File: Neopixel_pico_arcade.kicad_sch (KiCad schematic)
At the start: 15 parts, among them J1 SWD_connector, J2 NES_controller_connector, J3 USB_C_Receptacle_USB2.0, Q1 2N7002, U1 RP2040_Stamp, U2 SN74LV1T34DBV, U3 SRV05-4HTG-D

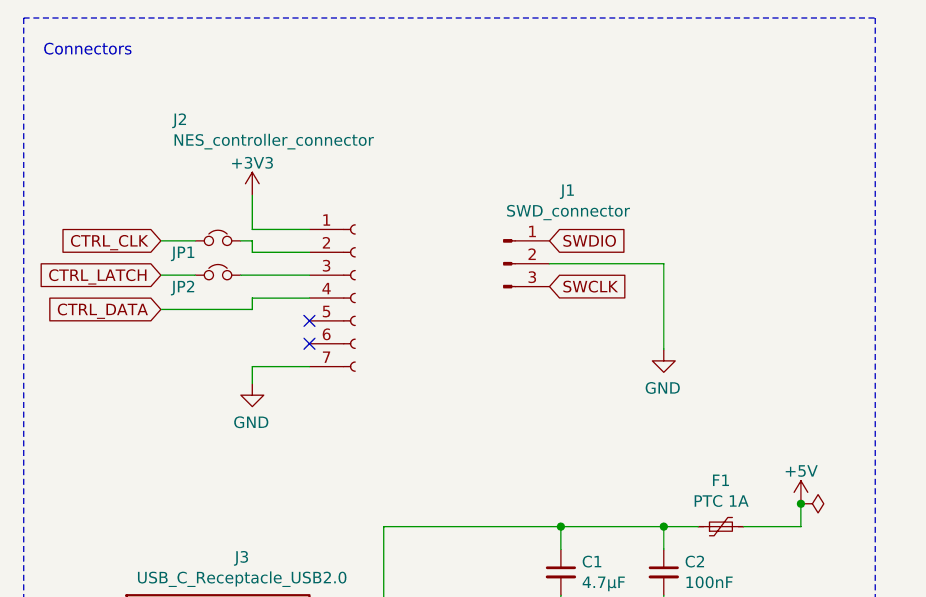
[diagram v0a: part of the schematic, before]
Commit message: Adds custom schematic symbol for NES controller connector
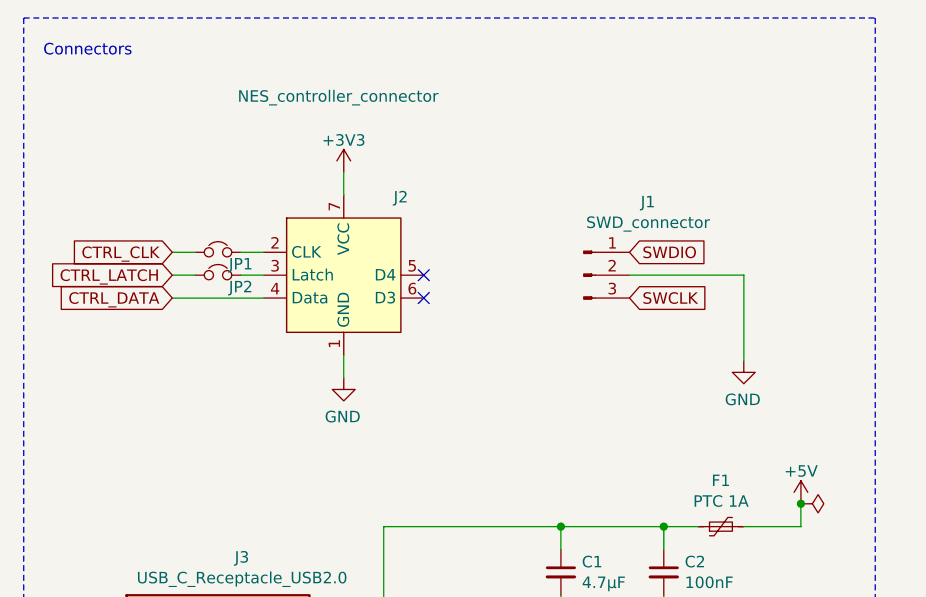
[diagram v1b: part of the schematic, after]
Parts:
- removed J2: NES_controller_connector, symbol Connector:Conn_01x07_Female
- added J2: NES_controller_connector, symbol Neopixel_pico_arcade:NES_controller_connector
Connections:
- net +3V3: now also J2.7 (VCC)
- net CTRL_DATA: now also J2.4 (Data)
- net GND: now also J2.1 (GND)
- net at JP1.2: now also J2.2 (CLK)
- net at JP2.2: now also J2.3 (Latch)
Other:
- moved on the sheet: J1, JP1

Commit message: Adds footprint for the NES controller connector
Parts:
- J2: footprint (none) -> Neopixel_pico_arcade:NES_Controller_connector
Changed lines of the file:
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@@
     (property "Reference" "J2" (id 0) (at 60.96 38.3244 0))
     (property "Value" "NES_controller_connector" (id 1) (at 53.975 27.1295 0))
-    (property "Footprint" "" (id 2) (at 54.61 46.99 0)
+    (property "Footprint" "Neopixel_pico_arcade:NES_Controller_connector" (id 2) (at 54.61 46.99 0)
       (effects (font (size 1.27 1.27)) hide)
     )
@@
     )
     (path "/0d864839-2792-4de0-80be-2a96e9fb5773"
-      (reference "J2") (unit 1) (value "NES_controller_connector") (footprint "")
+      (reference "J2") (unit 1) (value "NES_controller_connector") (footprint "Neopixel_pico_arcade:NES_Controller_connector")
     )
     (path "/6c963e39-9c66-450d-9ace-cb36b00aa8c0"

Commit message: Reassociates RP2040 stamp to the footprint
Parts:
- U1: footprint RP2040_Stamp:RP2040_Stamp_SMD -> RP2040_stamp:RP2040_Stamp_SMD
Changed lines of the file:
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@@
     (property "Reference" "U1" (id 0) (at 158.75 36.7242 0))
     (property "Value" "RP2040_Stamp" (id 1) (at 158.75 39.4993 0))
-    (property "Footprint" "RP2040_Stamp:RP2040_Stamp_SMD" (id 2) (at 158.75 123.19 0)
+    (property "Footprint" "RP2040_stamp:RP2040_Stamp_SMD" (id 2) (at 158.75 123.19 0)
       (effects (font (size 1.27 1.27)) hide)
     )
@@
     )
     (path "/99fe8e35-e5c1-4239-bd41-6a284ef403a7"
-      (reference "U1") (unit 1) (value "RP2040_Stamp") (footprint "RP2040_Stamp:RP2040_Stamp_SMD")
+      (reference "U1") (unit 1) (value "RP2040_Stamp") (footprint "RP2040_stamp:RP2040_Stamp_SMD")
     )
     (path "/9cc9bd3c-cb16-401b-a7ae-599f0e3ee9ec"

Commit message: Adds footprint for GTC USB4105 USB type C connector
This connector is for USB2.0 and power delivery only.

Datasheet is available at https://gct.co/files/specs/usb4105-spec.pdf
and drawings at https://gct.co/files/drawings/usb4105.pdf
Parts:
- J3: footprint Neopixel_pico_arcade:USB_C_Receptacle_JAE_DX07S016JA1 -> Neopixel_pico_arcade:USB_C_Receptacle_USB_2_GTC_USB4105
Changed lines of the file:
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@@
     (property "Reference" "J3" (id 0) (at 43.307 78.3398 0))
     (property "Value" "USB_C_Receptacle_USB2.0" (id 1) (at 43.307 80.6385 0))
-    (property "Footprint" "Neopixel_pico_arcade:USB_C_Receptacle_JAE_DX07S016JA1" (id 2) (at 44.45 100.33 0)
+    (property "Footprint" "Neopixel_pico_arcade:USB_C_Receptacle_USB_2_GTC_USB4105" (id 2) (at 44.45 100.33 0)
       (effects (font (size 1.27 1.27)) hide)
     )
@@
     )
     (path "/6c963e39-9c66-450d-9ace-cb36b00aa8c0"
-      (reference "J3") (unit 1) (value "USB_C_Receptacle_USB2.0") (footprint "Neopixel_pico_arcade:USB_C_Receptacle_JAE_DX07S016JA1")
+      (reference "J3") (unit 1) (value "USB_C_Receptacle_USB2.0") (footprint "Neopixel_pico_arcade:USB_C_Receptacle_USB_2_GTC_USB4105")
     )
     (path "/a9c99e6b-55b1-4adc-8611-0aea35c1c656"

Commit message: Adds project name and revision to schematics
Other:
- title: (none) -> Neopixel pico arcade
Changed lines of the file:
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@@
 (kicad_sch (version 20210621) (generator eeschema)
   (paper "A4")
+  (title_block
+    (title "Neopixel pico arcade")
+    (rev "1.0")
+  )
   (junction (at 36.83 127) (diameter 1.016) (color 0 0 0 0))
   (junction (at 57.15 100.33) (diameter 1.016) (color 0 0 0 0))

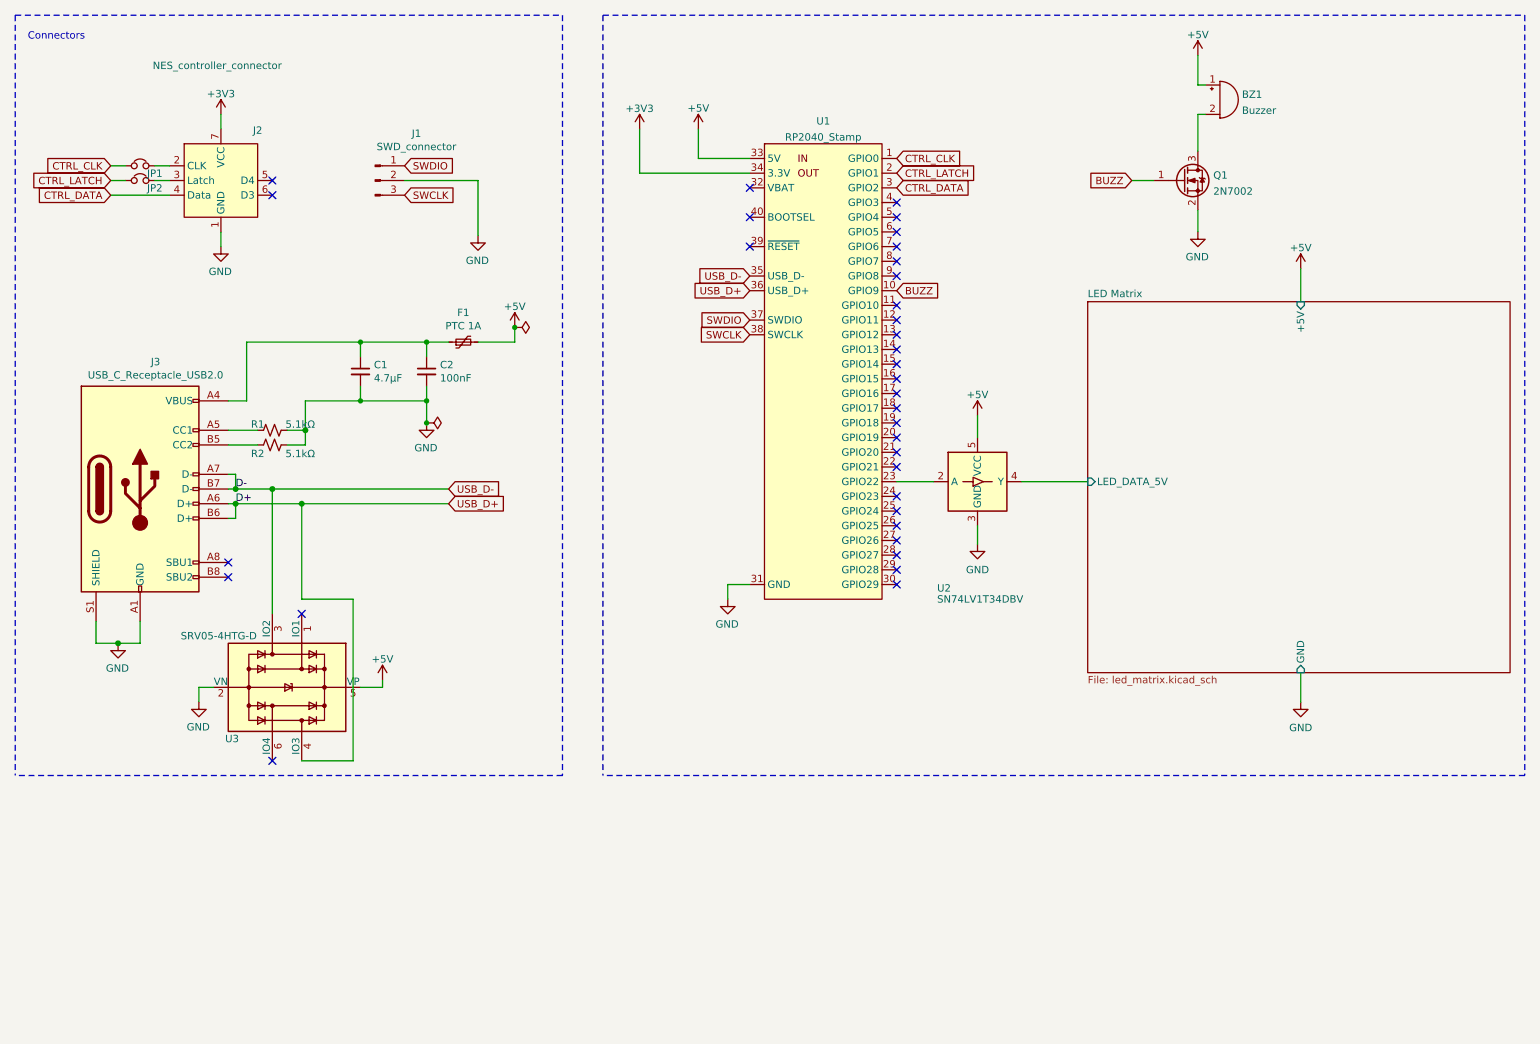
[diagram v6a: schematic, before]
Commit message: Adds mounting holes to schematics
These are connected to ground, but will have pads only on once the
bottom so the exposed pad on top doesn't interfere with the face where
the LEDs are.
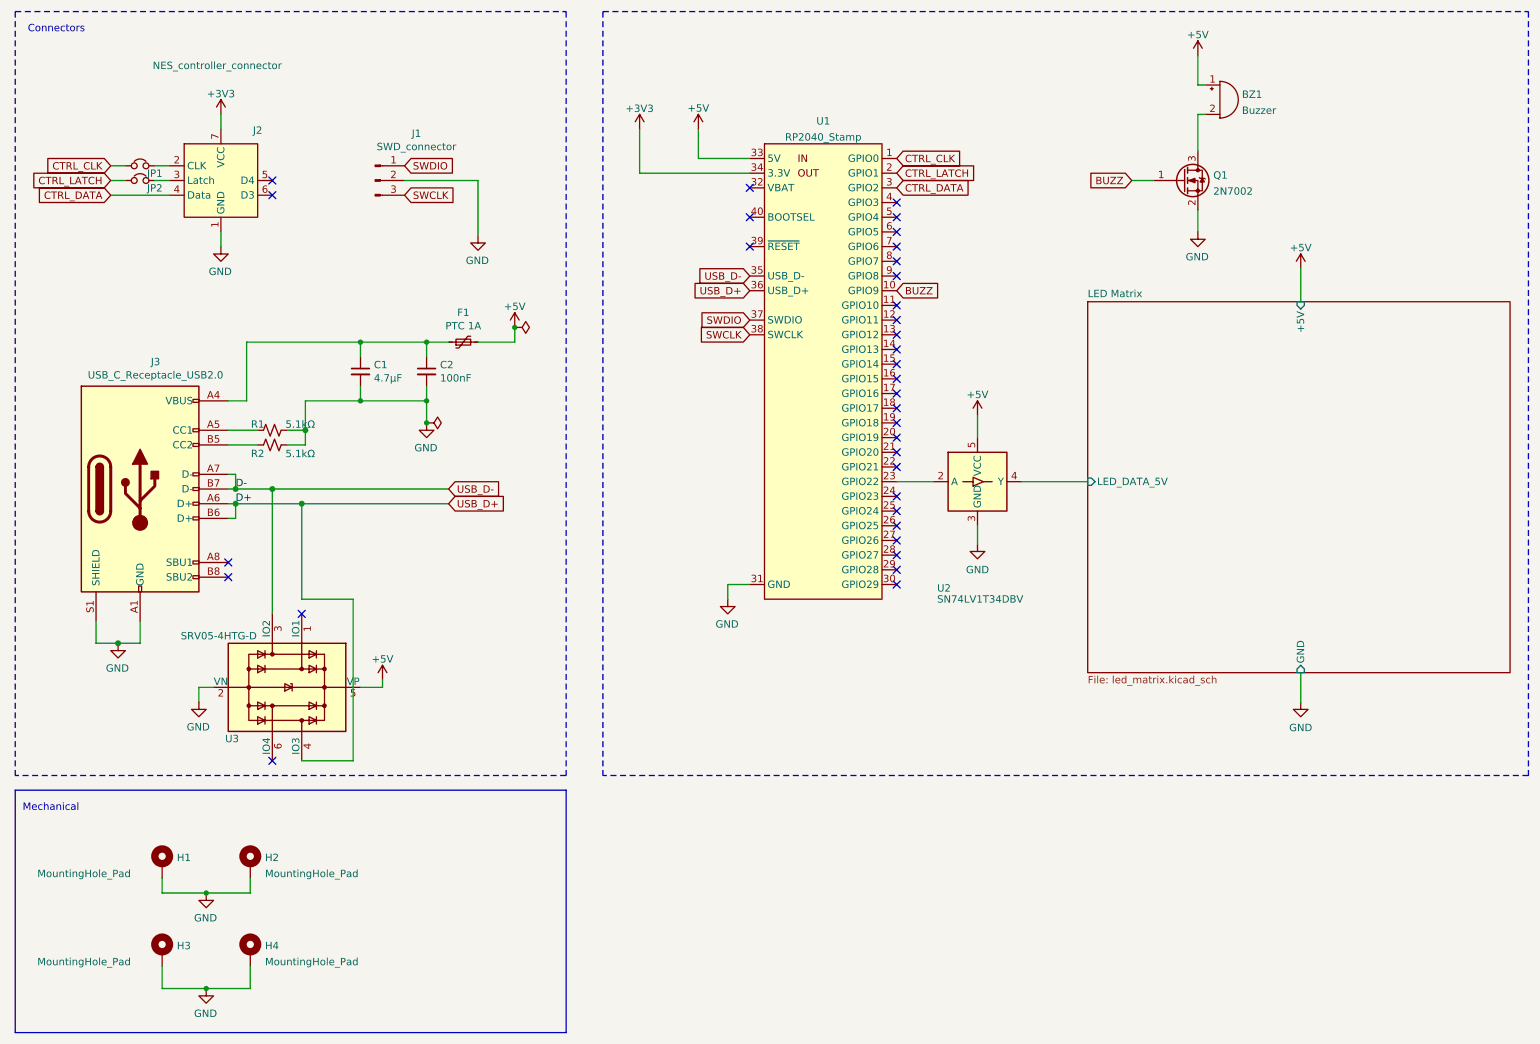
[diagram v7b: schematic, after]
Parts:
- added H1, H2, H3, H4: MountingHole_Pad, MountingHole:MountingHole_3.2mm_M3_ISO7380_Pad_TopOnly, symbol Mechanical:MountingHole_Pad
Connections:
- net GND: now also H1.1, H2.1, H3.1, H4.1
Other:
- note added: "Mechanical"
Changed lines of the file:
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@@
   )
   (junction (at 36.83 127) (diameter 1.016) (color 0 0 0 0))
+  (junction (at 52.07 170.18) (diameter 0) (color 0 0 0 0))
+  (junction (at 52.07 186.69) (diameter 0) (color 0 0 0 0))
   (junction (at 57.15 100.33) (diameter 1.016) (color 0 0 0 0))
   (junction (at 57.15 102.87) (diameter 1.016) (color 0 0 0 0))
@@
     (stroke (width 0) (type default) (color 0 0 0 0))
   )
+  (wire (pts (xy 44.45 167.64) (xy 44.45 170.18))
+    (stroke (width 0) (type default) (color 0 0 0 0))
+  )
+  (wire (pts (xy 44.45 170.18) (xy 52.07 170.18))
+    (stroke (width 0) (type default) (color 0 0 0 0))
+  )
+  (wire (pts (xy 44.45 182.88) (xy 44.45 186.69))
+    (stroke (width 0) (type default) (color 0 0 0 0))
+  )
+  (wire (pts (xy 44.45 186.69) (xy 52.07 186.69))
+    (stroke (width 0) (type default) (color 0 0 0 0))
+  )
   (wire (pts (xy 50.8 134.62) (xy 50.8 137.16))
     (stroke (width 0) (type solid) (color 0 0 0 0))
@@
     (stroke (width 0) (type default) (color 0 0 0 0))
   )
+  (wire (pts (xy 59.69 167.64) (xy 59.69 170.18))
+    (stroke (width 0) (type default) (color 0 0 0 0))
+  )
+  (wire (pts (xy 59.69 170.18) (xy 52.07 170.18))
+    (stroke (width 0) (type default) (color 0 0 0 0))
+  )
+  (wire (pts (xy 59.69 182.88) (xy 59.69 186.69))
+    (stroke (width 0) (type default) (color 0 0 0 0))
+  )
+  (wire (pts (xy 59.69 186.69) (xy 52.07 186.69))
+    (stroke (width 0) (type default) (color 0 0 0 0))
+  )
   (wire (pts (xy 63.5 100.33) (xy 63.5 121.92))
     (stroke (width 0) (type solid) (color 0 0 0 0))
@@
     (stroke (width 0) (type default) (color 0 0 0 0))
   )
-  (polyline (pts (xy 19.05 18.415) (xy 19.05 149.86))
+  (polyline (pts (xy 19.05 17.78) (xy 19.05 149.86))
     (stroke (width 0) (type dash) (color 0 0 0 0))
   )
-  (polyline (pts (xy 19.05 18.415) (xy 113.665 18.415))
+  (polyline (pts (xy 19.05 17.78) (xy 114.3 17.78))
     (stroke (width 0) (type dash) (color 0 0 0 0))
   )
-  (polyline (pts (xy 113.665 18.415) (xy 113.665 149.86))
+  (polyline (pts (xy 19.05 152.4) (xy 19.05 194.31))
+    (stroke (width 0) (type default) (color 0 0 0 0))
+  )
+  (polyline (pts (xy 19.05 152.4) (xy 114.3 152.4))
+    (stroke (width 0) (type default) (color 0 0 0 0))
+  )
+  (polyline (pts (xy 114.3 17.78) (xy 114.3 149.86))
     (stroke (width 0) (type dash) (color 0 0 0 0))
   )
-  (polyline (pts (xy 113.665 149.86) (xy 19.05 149.86))
+  (polyline (pts (xy 114.3 149.86) (xy 19.05 149.86))
     (stroke (width 0) (type dash) (color 0 0 0 0))
   )
-  (polyline (pts (xy 120.65 18.415) (xy 120.65 149.86))
+  (polyline (pts (xy 114.3 152.4) (xy 114.3 194.31))
+    (stroke (width 0) (type default) (color 0 0 0 0))
+  )
+  (polyline (pts (xy 114.3 194.31) (xy 19.05 194.31))
+    (stroke (width 0) (type default) (color 0 0 0 0))
+  )
+  (polyline (pts (xy 120.65 17.78) (xy 120.65 149.86))
     (stroke (width 0) (type dash) (color 0 0 0 0))
   )
-  (polyline (pts (xy 120.65 18.415) (xy 280.035 18.415))
+  (polyline (pts (xy 120.65 17.78) (xy 280.67 17.78))
     (stroke (width 0) (type dash) (color 0 0 0 0))
   )
-  (polyline (pts (xy 280.035 18.415) (xy 280.035 149.86))
+  (polyline (pts (xy 280.67 17.78) (xy 280.67 149.86))
     (stroke (width 0) (type dash) (color 0 0 0 0))
   )
-  (polyline (pts (xy 280.035 149.86) (xy 120.65 149.86))
+  (polyline (pts (xy 280.67 149.86) (xy 120.65 149.86))
     (stroke (width 0) (type dash) (color 0 0 0 0))
   )
-  (text "Connectors" (at 31.115 22.86 180)
+  (text "Mechanical" (at 20.32 156.21 0)
+    (effects (font (size 1.27 1.27)) (justify left bottom))
+  )
+  (text "Connectors" (at 31.115 21.59 180)
     (effects (font (size 1.27 1.27)) (justify right bottom))
   )
@@
     (pin "1")
   )
+  (symbol (lib_id "power:GND") (at 52.07 170.18 0) (mirror y) (unit 1)
+    (in_bom yes) (on_board yes)
+    (property "Reference" "#PWR01" (id 0) (at 52.07 176.53 0)
+      (effects (font (size 1.27 1.27)) hide)
+    )
+    (property "Value" "GND" (id 1) (at 51.9557 174.5044 0))
+    (property "Footprint" "" (id 2) (at 52.07 170.18 0)
+      (effects (font (size 1.27 1.27)) hide)
+    )
+    (property "Datasheet" "" (id 3) (at 52.07 170.18 0)
+      (effects (font (size 1.27 1.27)) hide)
+    )
+    (pin "1")
+  )
+  (symbol (lib_id "power:GND") (at 52.07 186.69 0) (mirror y) (unit 1)
+    (in_bom yes) (on_board yes)
+    (property "Reference" "#PWR04" (id 0) (at 52.07 193.04 0)
+      (effects (font (size 1.27 1.27)) hide)
+    )
+    (property "Value" "GND" (id 1) (at 51.9557 191.0144 0))
+    (property "Footprint" "" (id 2) (at 52.07 186.69 0)
+      (effects (font (size 1.27 1.27)) hide)
+    )
+    (property "Datasheet" "" (id 3) (at 52.07 186.69 0)
+      (effects (font (size 1.27 1.27)) hide)
+    )
+    (pin "1")
+  )
   (symbol (lib_id "power:GND") (at 54.61 58.42 0) (mirror y) (unit 1)
     (in_bom yes) (on_board yes)
@@
     (pin "1")
     (pin "2")
+  )
+  (symbol (lib_id "Mechanical:MountingHole_Pad") (at 44.45 165.1 0) (unit 1)
+    (in_bom yes) (on_board yes)
+    (property "Reference" "H1" (id 0) (at 46.9901 164.0645 0)
+      (effects (font (size 1.27 1.27)) (justify left))
+    )
+    (property "Value" "MountingHole_Pad" (id 1) (at 22.8601 166.8396 0)
+      (effects (font (size 1.27 1.27)) (justify left))
+    )
+    (property "Footprint" "MountingHole:MountingHole_3.2mm_M3_ISO7380_Pad_TopOnly" (id 2) (at 44.45 165.1 0)
+      (effects (font (size 1.27 1.27)) hide)
+    )
+    (property "Datasheet" "~" (id 3) (at 44.45 165.1 0)
+      (effects (font (size 1.27 1.27)) hide)
+    )
+    (pin "1")
+  )
+  (symbol (lib_id "Mechanical:MountingHole_Pad") (at 44.45 180.34 0) (unit 1)
+    (in_bom yes) (on_board yes)
+    (property "Reference" "H3" (id 0) (at 46.9901 179.3045 0)
+      (effects (font (size 1.27 1.27)) (justify left))
+    )
+    (property "Value" "MountingHole_Pad" (id 1) (at 22.8601 182.0796 0)
+      (effects (font (size 1.27 1.27)) (justify left))
+    )
+    (property "Footprint" "MountingHole:MountingHole_3.2mm_M3_ISO7380_Pad_TopOnly" (id 2) (at 44.45 180.34 0)
+      (effects (font (size 1.27 1.27)) hide)
+    )
+    (property "Datasheet" "~" (id 3) (at 44.45 180.34 0)
+      (effects (font (size 1.27 1.27)) hide)
+    )
+    (pin "1")
+  )
+  (symbol (lib_id "Mechanical:MountingHole_Pad") (at 59.69 165.1 0) (unit 1)
+    (in_bom yes) (on_board yes) (fields_autoplaced)
+    (property "Reference" "H2" (id 0) (at 62.2301 164.0645 0)
+      (effects (font (size 1.27 1.27)) (justify left))
+    )
+    (property "Value" "MountingHole_Pad" (id 1) (at 62.2301 166.8396 0)
+      (effects (font (size 1.27 1.27)) (justify left))
+    )
+    (property "Footprint" "MountingHole:MountingHole_3.2mm_M3_ISO7380_Pad_TopOnly" (id 2) (at 59.69 165.1 0)
+      (effects (font (size 1.27 1.27)) hide)
+    )
+    (property "Datasheet" "~" (id 3) (at 59.69 165.1 0)
+      (effects (font (size 1.27 1.27)) hide)
+    )
+    (pin "1")
+  )
+  (symbol (lib_id "Mechanical:MountingHole_Pad") (at 59.69 180.34 0) (unit 1)
+    (in_bom yes) (on_board yes) (fields_autoplaced)
+    (property "Reference" "H4" (id 0) (at 62.2301 179.3045 0)
+      (effects (font (size 1.27 1.27)) (justify left))
+    )
+    (property "Value" "MountingHole_Pad" (id 1) (at 62.2301 182.0796 0)
+      (effects (font (size 1.27 1.27)) (justify left))
+    )
+    (property "Footprint" "MountingHole:MountingHole_3.2mm_M3_ISO7380_Pad_TopOnly" (id 2) (at 59.69 180.34 0)
+      (effects (font (size 1.27 1.27)) hide)
+    )
+    (property "Datasheet" "~" (id 3) (at 59.69 180.34 0)
+      (effects (font (size 1.27 1.27)) hide)
+    )
+    (pin "1")
   )
   (symbol (lib_id "Connector:Conn_01x03_Male") (at 81.28 46.99 0) (unit 1)
@@
       (reference "#FLG0101") (unit 1) (value "PWR_FLAG") (footprint "")
     )
+    (path "/b9fbd855-786e-41b8-a228-ad0c8b4682ba"
+      (reference "#PWR01") (unit 1) (value "GND") (footprint "")
+    )
     (path "/1729631f-de18-4c58-a71d-335612619424"
       (reference "#PWR02") (unit 1) (value "+3V3") (footprint "")
@@
       (reference "#PWR03") (unit 1) (value "+3V3") (footprint "")
     )
+    (path "/3a3bb1b7-b91a-4480-af80-dd62b0c3c9e4"
+      (reference "#PWR04") (unit 1) (value "GND") (footprint "")
+    )
     (path "/1556db3c-27c0-41bc-8714-1a11047a4079"
       (reference "#PWR05") (unit 1) (value "GND") (footprint "")
@@
       (reference "F1") (unit 1) (value "PTC 1A") (footprint "Neopixel_pico_arcade:Belfuse_0ZCJ")
     )
+    (path "/7a8c1597-e0df-452f-99e4-b1beaee06a70"
+      (reference "H1") (unit 1) (value "MountingHole_Pad") (footprint "MountingHole:MountingHole_3.2mm_M3_ISO7380_Pad_TopOnly")
+    )
+    (path "/f4638d81-26f6-4649-ab07-f00262b31eaa"
+      (reference "H2") (unit 1) (value "MountingHole_Pad") (footprint "MountingHole:MountingHole_3.2mm_M3_ISO7380_Pad_TopOnly")
+    )
+    (path "/7a66ec64-5407-42aa-9b95-71620daa6221"
+      (reference "H3") (unit 1) (value "MountingHole_Pad") (footprint "MountingHole:MountingHole_3.2mm_M3_ISO7380_Pad_TopOnly")
+    )
+    (path "/4df7c262-40d8-4fb2-ad74-a15b5a3c3424"
+      (reference "H4") (unit 1) (value "MountingHole_Pad") (footprint "MountingHole:MountingHole_3.2mm_M3_ISO7380_Pad_TopOnly")
+    )
     (path "/2d555828-831d-4418-8791-29126d2f97c5"
